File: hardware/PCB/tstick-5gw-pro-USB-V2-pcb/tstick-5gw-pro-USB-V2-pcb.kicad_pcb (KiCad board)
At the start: 4 copper layers, 53.3 x 25.4 mm, 62 parts, among them J1 USB_C_Receptacle_USB2.0, Q1 BSS138, Q2 BSS138, Q3 BSS138, SW1 PTS810 SJM Switch, SW2 PTS810 SJM Switch, U1 USBLC6-2P6, U2 MCP73871, U3 NCP167AMX330TBG, U4 NCP167AMX180TBG

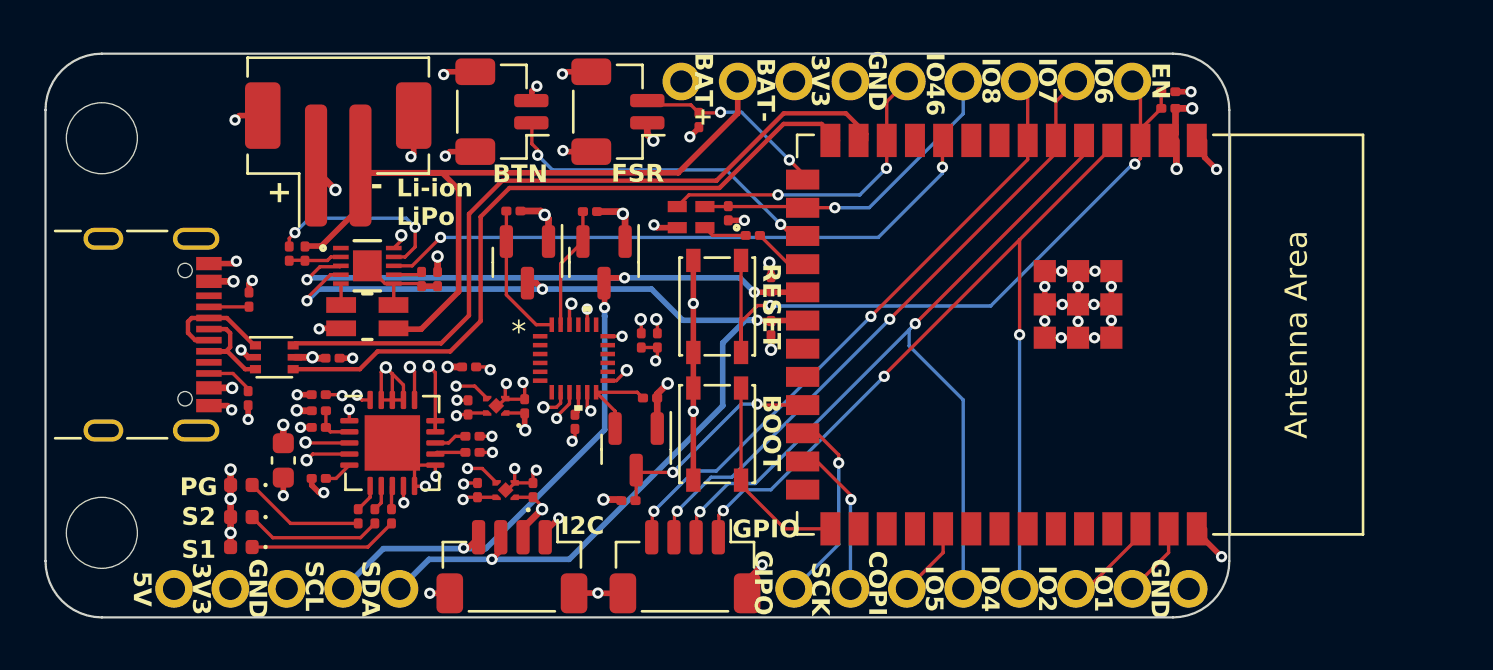
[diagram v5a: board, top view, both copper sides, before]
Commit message: updated pcb BOM, switched buttons to smaller 3x2mm buttons
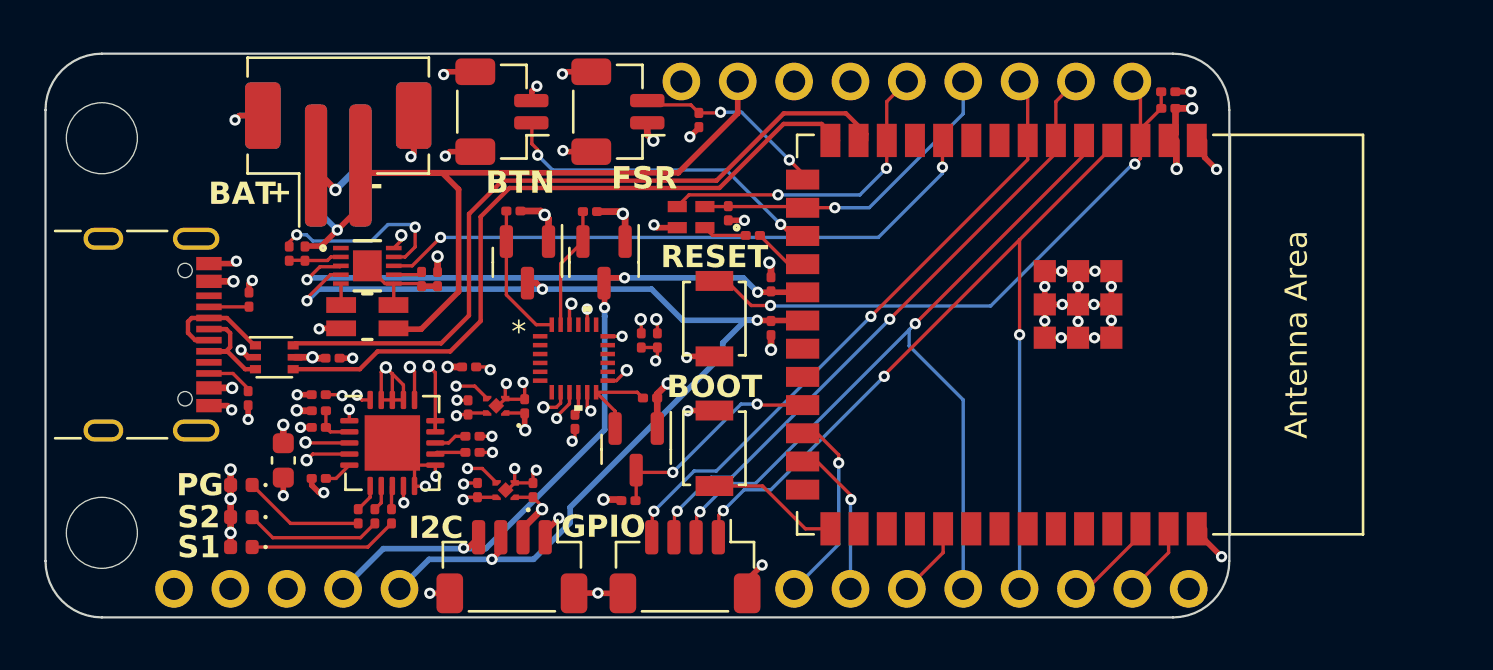
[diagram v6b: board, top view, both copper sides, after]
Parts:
- added BT2: JST-PH-1x02-2.000mm, Connector_JST:JST_PH_B2B-PH-SM4-TB_1x02-1MP_P2.00mm_Vertical, B.Cu at (105.9, 52.8)
- SW1, SW2: value PTS810 SJM Switch -> B3U-1000P; footprint Button_Switch_SMD:SW_SPST_PTS810 -> Button_Switch_SMD:SW_SPST_B3U-1000P
- moved SW1 0.65 mm to (122.8, 66.0), turned to 90 degrees
- moved SW2 0.56 mm to (122.8, 60.2)
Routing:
- net GND: track 76.7 -> 72.6 mm
- net /EN: track 32.8 -> 28.6 mm
- net -BATT: track 37.1 -> 40.4 mm, vias 0 -> 1
- net /IO0: track 9.34 -> 6.37 mm
- net +BATT: track 8.65 -> 10.2 mm
- net /SDA: track 50.3 -> 49.4 mm
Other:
- board text added: "BAT"
- board text added: "BTN IO9"
- board text added: "Custom T-Stick Board v1.1 2023-11 IDMIL McGill University Albert Niyonsenga"
- board text added: "FSR IO3"
- board text removed: "ANALOG/ BTN IN IO9"
- board text removed: "Custom T-Stick Board v1.0 2023-10 IDMIL McGill University Albert Niyonsenga"
- board text removed: "FSR IN IO3"
- board text removed: "Li-ion LiPo"
- board text removed: "SCL = IO11 SDA = IO12 LED DATA = IO10 LED EXTRA = IO08 LED POWER = IO46 IMU INT = IO21 FUEL GAUGE INT = IO17"

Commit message: updated board flash size, added button interrupt, removed serial print
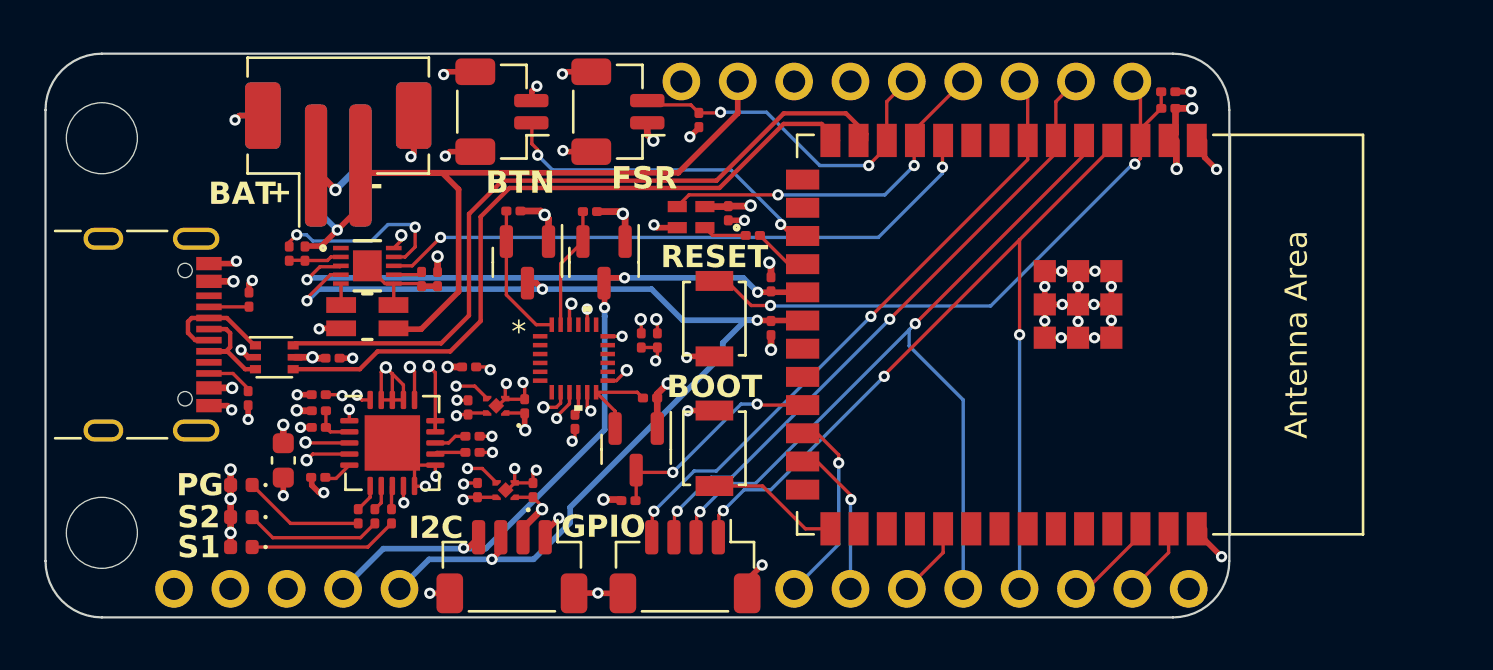
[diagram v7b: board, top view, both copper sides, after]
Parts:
- removed TH2: 10k, Resistor_SMD:R_0201_0603Metric
- added R9: 10k, Resistor_SMD:R_0201_0603Metric, F.Cu at (105.0, 67.3)
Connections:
- ANG1 pad 2: /IO3 -> /IO8
- BOARDLAYOUT1 pad 6: /IO46 -> /IO18
- C13 pad 1: /IO46 -> +3V3
- PWLED1 pad 2: /IO46 -> +3V3
- PWLED1 pad 3: /IO8 -> /IO18
- R1 pad 1: /IO3 -> /IO8
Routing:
- net /IO18: track 0.00 -> 16.1 mm, vias 0 -> 2
- net /IO46: track 15.1 -> 0.01 mm, vias 1 -> 0
- net /IO3: track 8.99 -> 0.21 mm, vias 2 -> 0
- net +3V3: track 9.83 -> 11.9 mm, vias 7 -> 8
- net /IO8: track 14.4 -> 15.7 mm

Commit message: removed some LED code, updated schematic, removed choke resistor from both board and BOM
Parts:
- removed R8: 300, Resistor_SMD:R_0201_0603Metric
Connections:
- PWLED1 pad 1: Net-(PWLED1-DIN) -> /IO10
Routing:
- net /IO10: track 3.78 -> 6.41 mm
- net Net-(PWLED1-DIN): track 1.98 -> 0.00 mm
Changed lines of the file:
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@@
   (net 82 "/D+")
   (net 83 "/D-")
-  (net 84 "Net-(PWLED1-DIN)")
   (footprint "NCP167AMX330TBG-footprints:XDFN4_1X1_711AJ_ONS" (layer "F.Cu")
     (at 113.0186 64.12615 180)
@@
       (stroke (width 0.0254) (type solid)) (fill none) (layer "F.Fab"))
     (pad "1" smd rect (at -0.623001 -0.475 180) (size 0.8636 0.508) (layers "F.Cu" "F.Paste" "F.Mask")
-      (net 84 "Net-(PWLED1-DIN)") (pinfunction "DIN") (pintype "unspecified"))
+      (net 65 "/IO10") (pinfunction "DIN") (pintype "unspecified"))
     (pad "2" smd rect (at -0.623001 0.475 180) (size 0.8636 0.508) (layers "F.Cu" "F.Paste" "F.Mask")
       (net 5 "+3V3") (pinfunction "VDD") (pintype "unspecified"))
@@
     )
   )
-  (footprint "Resistor_SMD:R_0201_0603Metric" (layer "F.Cu")
-    (at 124.58 56.45 180)
-    (descr "Resistor SMD 0201 (0603 Metric), square (rectangular) end terminal, IPC_7351 nominal, (Body size source: https://www.vishay.com/docs/20052/crcw0201e3.pdf), generated with kicad-footprint-generator")
-    (tags "resistor")
-    (property "Description Value Pkg" "300 Ohms ±1% 0.05W, 1/20W Chip Resistor 0201 (0603 Metric) Thick Film")
-    (property "Manufacturer" "Panasonic Electronic Components")
-    (property "Mfg Part #" "ERJ-1GNF3000C")
-    (property "Sheetfile" "tstick-5gw-pro-USB-V2-pcb.kicad_sch")
-    (property "Sheetname" "")
-    (property "ki_description" "Resistor, US symbol")
-    (property "ki_keywords" "R res resistor")
-    (property "mpn" "ERJ-1GNF3000C")
-    (attr smd)
-    (fp_text reference "R8" (at 0 -1.05) (layer "F.SilkS") hide
-        (effects (font (size 1 1) (thickness 0.15)))
-    )
-    (fp_text value "300" (at 0 1.05) (layer "F.Fab")
-        (effects (font (size 1 1) (thickness 0.15)))
-    )
-    (fp_text user "${REFERENCE}" (at 0 -0.68) (layer "F.Fab")
-        (effects (font (size 0.25 0.25) (thickness 0.04)))
-    )
-    (fp_line (start -0.7 -0.35) (end 0.7 -0.35)
-      (stroke (width 0.05) (type solid)) (layer "F.CrtYd"))
-    (fp_line (start -0.7 0.35) (end -0.7 -0.35)
-      (stroke (width 0.05) (type solid)) (layer "F.CrtYd"))
-    (fp_line (start 0.7 -0.35) (end 0.7 0.35)
-      (stroke (width 0.05) (type solid)) (layer "F.CrtYd"))
-    (fp_line (start 0.7 0.35) (end -0.7 0.35)
-      (stroke (width 0.05) (type solid)) (layer "F.CrtYd"))
-    (fp_line (start -0.3 -0.15) (end 0.3 -0.15)
-      (stroke (width 0.1) (type solid)) (layer "F.Fab"))
-    (fp_line (start -0.3 0.15) (end -0.3 -0.15)
-      (stroke (width 0.1) (type solid)) (layer "F.Fab"))
-    (fp_line (start 0.3 -0.15) (end 0.3 0.15)
-      (stroke (width 0.1) (type solid)) (layer "F.Fab"))
-    (fp_line (start 0.3 0.15) (end -0.3 0.15)
-      (stroke (width 0.1) (type solid)) (layer "F.Fab"))
-    (pad "" smd roundrect (at -0.345 0 180) (size 0.318 0.36) (layers "F.Paste") (roundrect_rratio 0.25))
-    (pad "" smd roundrect (at 0.345 0 180) (size 0.318 0.36) (layers "F.Paste") (roundrect_rratio 0.25))
-    (pad "1" smd roundrect (at -0.32 0 180) (size 0.46 0.4) (layers "F.Cu" "F.Mask") (roundrect_rratio 0.25)
-      (net 65 "/IO10") (pintype "passive"))
-    (pad "2" smd roundrect (at 0.32 0 180) (size 0.46 0.4) (layers "F.Cu" "F.Mask") (roundrect_rratio 0.25)
-      (net 84 "Net-(PWLED1-DIN)") (pintype "passive"))
-    (model "${KICAD6_3DMODEL_DIR}/Resistor_SMD.3dshapes/R_0201_0603Metric.wrl"
-      (offset (xyz 0 0 0))
-      (scale (xyz 1 1 1))
-      (rotate (xyz 0 0 0))
-    )
-  )
   (footprint "Capacitor_SMD:C_0201_0603Metric" (layer "F.Cu")
     (at 120.28 61.18 -90)
@@
   (via (at 114.8875 52.8349) (size 0.508) (drill 0.254) (layers "F.Cu" "B.Cu") (net 46))
   (via (at 125.835104 55.952022) (size 0.508) (drill 0.254) (layers "F.Cu" "B.Cu") (net 46))
-  (segment (start 123.6 53.5) (end 125.835104 55.735104) (width 0.1524) (layer "B.Cu") (net 46))
+  (segment (start 115.5526 53.5) (end 123.6 53.5) (width 0.1524) (layer "B.Cu") (net 46))
   (segment (start 114.8875 52.8349) (end 115.5526 53.5) (width 0.1524) (layer "B.Cu") (net 46))
   (segment (start 125.835104 55.735104) (end 125.835104 55.952022) (width 0.1524) (layer "B.Cu") (net 46))
-  (segment (start 115.5526 53.5) (end 123.6 53.5) (width 0.1524) (layer "B.Cu") (net 46))
+  (segment (start 123.6 53.5) (end 125.835104 55.735104) (width 0.1524) (layer "B.Cu") (net 46))
   (segment (start 108.4018 57.819101) (end 109.231799 57.819101) (width 0.1524) (layer "F.Cu") (net 47))
   (segment (start 133.125 53.375) (end 133.125 52.5491) (width 0.1524) (layer "F.Cu") (net 47))
@@
   (segment (start 131.7925 72.1025) (end 133.155 70.74) (width 0.1524) (layer "F.Cu") (net 63))
   (segment (start 133.155 70.74) (end 133.155 69.6691) (width 0.1524) (layer "F.Cu") (net 63))
+  (segment (start 122.421002 56.1) (end 122.771002 56.45) (width 0.1524) (layer "F.Cu") (net 65))
   (segment (start 126.4846 57.7441) (end 126.825 57.7441) (width 0.1524) (layer "F.Cu") (net 65))
-  (segment (start 124.9 56.45) (end 126.1941 57.7441) (width 0.1524) (layer "F.Cu") (net 65))
   (segment (start 126.1941 57.7441) (end 126.825 57.7441) (width 0.1524) (layer "F.Cu") (net 65))
+  (segment (start 124.9 56.45) (end 126.1941 57.7441) (width 0.1524) (layer "F.Cu") (net 65))
+  (segment (start 122.771002 56.45) (end 124.9 56.45) (width 0.1524) (layer "F.Cu") (net 65))
   (segment (start 126.1941 57.7441) (end 127.175 57.7441) (width 0.1524) (layer "F.Cu") (net 65))
   (segment (start 107.3375 63.8625) (end 106.9625 63.8625) (width 0.1524) (layer "F.Cu") (net 70))
@@
   (segment (start 99.459 61.1691) (end 100.073 61.1691) (width 0.2) (layer "F.Cu") (net 83))
   (segment (start 100.88285 60.1691) (end 100.073 60.1691) (width 0.2) (layer "F.Cu") (net 83))
-  (segment (start 122.421002 56.1) (end 122.771002 56.45) (width 0.1524) (layer "F.Cu") (net 84))
-  (segment (start 122.771002 56.45) (end 124.26 56.45) (width 0.1524) (layer "F.Cu") (net 84))
   (zone (net 6) (net_name "GND") (layer "In1.Cu") (name "GND") (hatch edge 0.5)
     (connect_pads (clearance 0.1524))
